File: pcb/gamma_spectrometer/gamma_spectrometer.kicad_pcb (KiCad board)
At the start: 4 copper layers, 45 x 45 mm, 186 parts, among them J101 DX07S024WJ3R400, Q201 IRLML0040, Q401 MMBTA42, Q402 MMBTA42, Q403 MMBTA42, T201 ATB322524-0110-T000, U101 LP5907MFX-3.3, U102 AMS1117-3.3, U103 FT231XQ, U104 TPS60400DBV, U201 max1847eee+, U202 TL431, U301 TL431, U302 STM32G474MET6, U303 W25Q64JVSSIQ, U401 AD8000YRDZ-REEL, Y301 ABM8G-16.000MHZ-4Y-T3

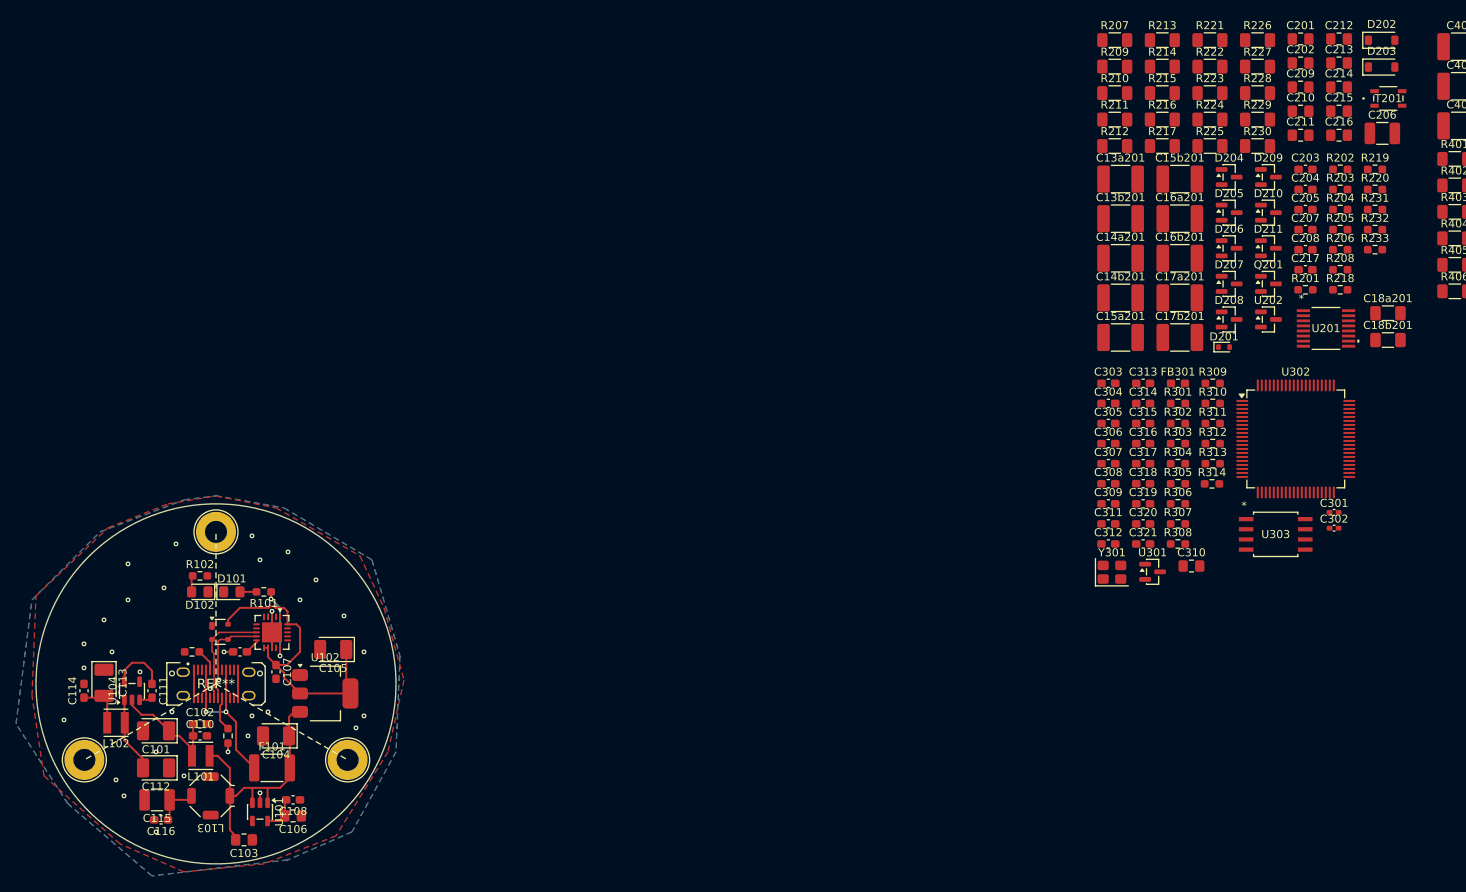
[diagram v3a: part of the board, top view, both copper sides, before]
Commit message: pcb: разводка HV + GND-полигоны + межплатная шина (HV/USB)
- HV-плата разведена (накопит. конденсаторы и монитор-делитель вынесены вниз),
  GND залит полигонами, паритет со схемой 0.
- USB: добавлен GND-план на In2.Cu (второй внутренний слой), сшивка.
- Межплатная шина цанг-пинов: по 13 пинов на HV и USB, выровнены на R20
  равным шагом 13° с разрывами под стойки (120°/240°); углы идентичны на
  обеих платах -> соосность через стек.
- DRC (headless, с заливкой зон): паритет со схемой 0 на обеих платах;
  остатки минорные (1-2 GND-хвоста, courtyard-грейзы пин/стойка, silk, REF**).

Co-Authored-By: Claude Opus 4.8 <noreply@anthropic.com>
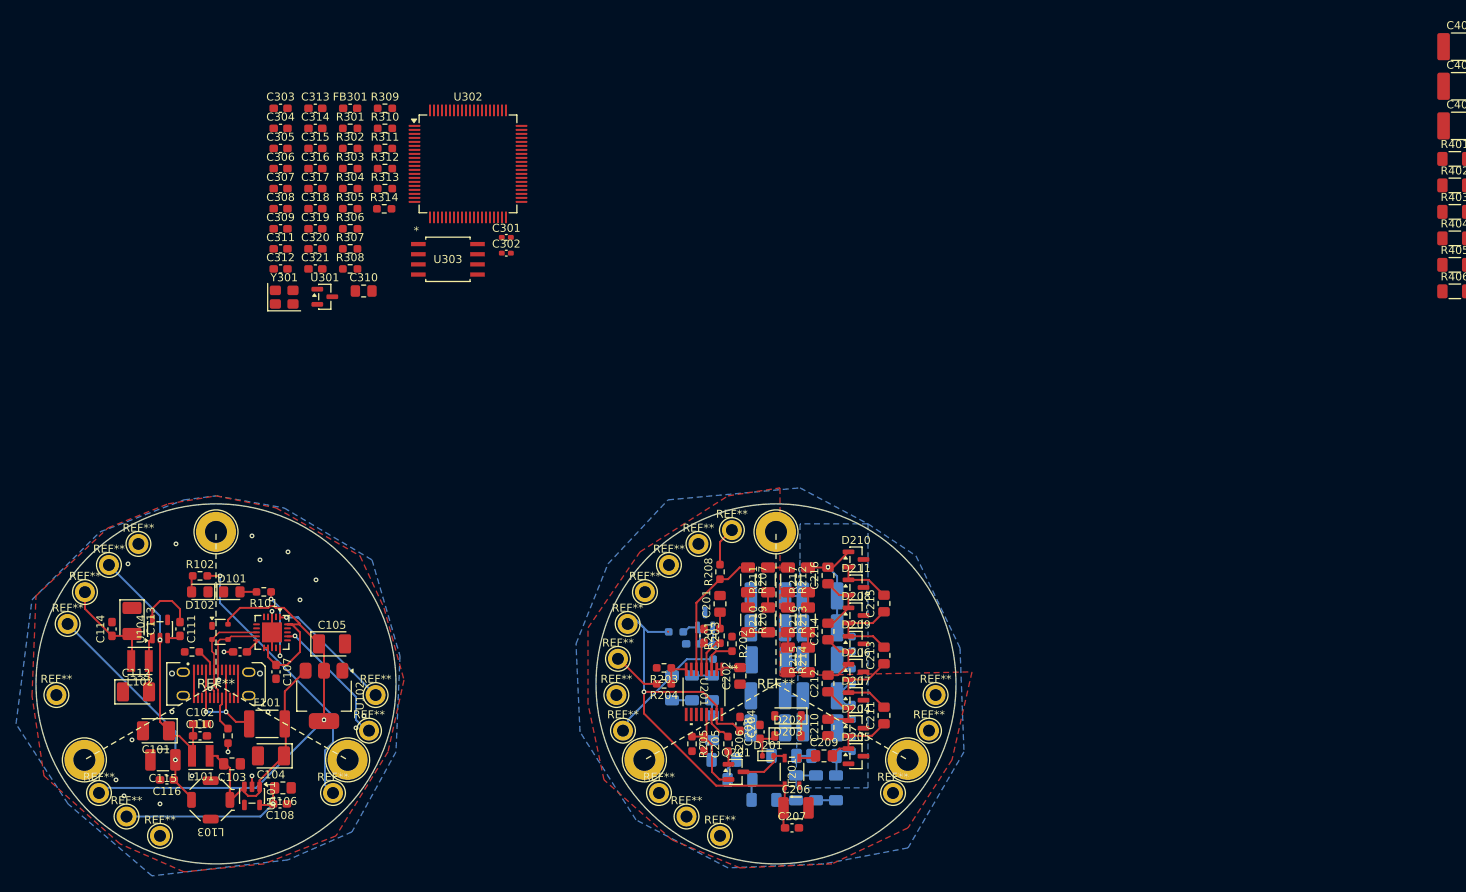
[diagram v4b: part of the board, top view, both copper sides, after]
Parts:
- added REF**: INTERCONNECT_PIN_D1.5, посадочные места:INTERCONNECT_PIN_D1.5, F.Cu at (156.6, 85.1)
- added REF**: INTERCONNECT_PIN_D1.5, посадочные места:INTERCONNECT_PIN_D1.5, F.Cu at (80.0, 101.4)
- added REF**: INTERCONNECT_PIN_D1.5, посадочные места:INTERCONNECT_PIN_D1.5, F.Cu at (114.6, 113.6)
- added REF**: INTERCONNECT_PIN_D1.5, посадочные места:INTERCONNECT_PIN_D1.5, F.Cu at (86.6, 85.1)
- added REF**: INTERCONNECT_PIN_D1.5, посадочные места:INTERCONNECT_PIN_D1.5, F.Cu at (150.9, 105.8)
- added REF**: INTERCONNECT_PIN_D1.5, посадочные места:INTERCONNECT_PIN_D1.5, F.Cu at (150.0, 101.4)
- added REF**: STANDOFF_M2.5_GND_x3_TRIANGLE, посадочные места:STANDOFF_M2.5_GND_x3_TRIANGLE, F.Cu at (170.0, 100.0)
- added REF**: INTERCONNECT_PIN_D1.5, посадочные места:INTERCONNECT_PIN_D1.5, F.Cu at (160.3, 82.5)
- added REF**: INTERCONNECT_PIN_D1.5, посадочные места:INTERCONNECT_PIN_D1.5, F.Cu at (190.0, 101.4)
- added REF**: INTERCONNECT_PIN_D1.5, посадочные места:INTERCONNECT_PIN_D1.5, F.Cu at (184.6, 113.6)
- added REF**: INTERCONNECT_PIN_D1.5, посадочные места:INTERCONNECT_PIN_D1.5, F.Cu at (120.0, 101.4)
- added REF**: INTERCONNECT_PIN_D1.5, посадочные места:INTERCONNECT_PIN_D1.5, F.Cu at (164.5, 80.8)
- added REF**: INTERCONNECT_PIN_D1.5, посадочные места:INTERCONNECT_PIN_D1.5, F.Cu at (88.8, 116.6)
- added REF**: INTERCONNECT_PIN_D1.5, посадочные места:INTERCONNECT_PIN_D1.5, F.Cu at (153.6, 88.5)
- added REF**: INTERCONNECT_PIN_D1.5, посадочные места:INTERCONNECT_PIN_D1.5, F.Cu at (81.5, 92.5)
- added REF**: INTERCONNECT_PIN_D1.5, посадочные места:INTERCONNECT_PIN_D1.5, F.Cu at (90.3, 82.5)
- added REF**: INTERCONNECT_PIN_D1.5, посадочные места:INTERCONNECT_PIN_D1.5, F.Cu at (189.1, 105.8)
- added REF**: INTERCONNECT_PIN_D1.5, посадочные места:INTERCONNECT_PIN_D1.5, F.Cu at (163.0, 119.0)
- added REF**: INTERCONNECT_PIN_D1.5, посадочные места:INTERCONNECT_PIN_D1.5, F.Cu at (150.2, 96.9)
- added REF**: INTERCONNECT_PIN_D1.5, посадочные места:INTERCONNECT_PIN_D1.5, F.Cu at (83.6, 88.5)
- added REF**: INTERCONNECT_PIN_D1.5, посадочные места:INTERCONNECT_PIN_D1.5, F.Cu at (158.8, 116.6)
- added REF**: INTERCONNECT_PIN_D1.5, посадочные места:INTERCONNECT_PIN_D1.5, F.Cu at (155.4, 113.6)
- added REF**: INTERCONNECT_PIN_D1.5, посадочные места:INTERCONNECT_PIN_D1.5, F.Cu at (85.4, 113.6)
- added REF**: INTERCONNECT_PIN_D1.5, посадочные места:INTERCONNECT_PIN_D1.5, F.Cu at (119.1, 105.8)
- added REF**: INTERCONNECT_PIN_D1.5, посадочные места:INTERCONNECT_PIN_D1.5, F.Cu at (93.0, 119.0)
- added REF**: INTERCONNECT_PIN_D1.5, посадочные места:INTERCONNECT_PIN_D1.5, F.Cu at (151.5, 92.5)
- C13a201, C13b201, C14a201, C14b201, C15a201, C15b201, C16a201, C16b201, C17a201, C17b201, C18a201, C18b201, C217, R218, R219, R220, R221, R222, R223, R224, R225, R226, R227, R228, R229, R230, R231, R232, R233, U202: moved to B.Cu
- moved D202 114.3 mm to (171.5, 106.5)
- moved T201 112.4 mm to (172.0, 111.0), turned to 90 degrees
- moved R226 112.0 mm to (163.5, 109.5), turned to 180 degrees
- moved C206 111.7 mm to (172.5, 115.5)
- moved D203 109.9 mm to (171.5, 104.0), turned to 180 degrees
- moved U303 109.0 mm to (129.0, 46.9)
- moved C310 109.0 mm to (118.5, 50.9)
- moved C313 109.0 mm to (112.4, 28.1)
- moved C314 109.0 mm to (112.4, 30.6)
- moved C315 109.0 mm to (112.4, 33.1)
- moved C316 109.0 mm to (112.4, 35.6)
- moved C317 109.0 mm to (112.4, 38.1)
- moved C318 109.0 mm to (112.4, 40.6)
- moved C319 109.0 mm to (112.4, 43.1)
- moved C320 109.0 mm to (112.4, 45.6)
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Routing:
- net +5V_HV: track 5.53 -> 88.5 mm, vias 0 -> 2
- net LED: track 0.00 -> 35.4 mm, vias 0 -> 1
- net +3.3V_D: track 38.9 -> 69.1 mm, vias 0 -> 1
- net +3.3V_A: track 4.49 -> 22.8 mm, vias 0 -> 1
- net +5V_A: track 16.1 -> 33.5 mm, vias 0 -> 1
- net UART_TX: track 0.00 -> 16.8 mm, vias 0 -> 1
- net Net-(U201-FB): track 0.00 -> 16.6 mm
- net Net-(C13a201-Pad1): track 0.00 -> 16.2 mm, vias 0 -> 1
- net UART_RX: track 0.00 -> 16.1 mm, vias 0 -> 1
- net HV_MONITOR: track 0.00 -> 15.5 mm
- net Net-(C211-Pad2): track 0.00 -> 12.1 mm
- net Net-(Q201-S): track 0.00 -> 11.7 mm
- net Net-(C213-Pad2): track 0.00 -> 11.7 mm
- net Net-(C209-Pad2): track 0.00 -> 9.08 mm
- net Net-(C214-Pad2): track 0.00 -> 8.10 mm
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- added copper zone on In2.Cu, net GND
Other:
- board size 45 x 45 mm -> 115 x 45 mm

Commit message: pcb: ВВ-зазоры 3 мм/кВ правилами DRC + 2 слоя + разводка делителя
Плата переведена 4 -> 2 слоя (ЛУТ-прототипы): на In1/In2 разводки не было,
удалены только зоны, связность не изменилась (178 несоединённых до и после).
Стек F.Cu / core FR4 1.51 / B.Cu = 1.60 мм. Побочно снят риск: под -1500 В
лежала сплошная земля через препрег 0.1 мм (15 кВ/мм), стало 0.99 кВ/мм.

Нормы ВВ-зазоров заданы правилами DRC (gamma_spectrometer.kicad_dru):
49 правил "ВВ-цепь <-> GND" по 3 мм на 1 кВ + 12 исключений. Потенциалы
посчитаны из топологии: рабочая точка делителя, порядок лестницы CW по
диодам (8 ступеней по 189 В), падения на выходном RC, цепочки ОС и монитора.
Зазоры 4.54 мм (CW_out, 1514 В) ... 0.43 мм. Ограничивают только пару с GND —
между соседними ступенями ВВ разность 150-190 В (принцип градиента).

Исключения: 12 компонентов по схеме соединяют ВВ-узел с землёй (T201, C210,
D205, C410, R412, C13b-C18b201, Q403). У них зазор задан корпусом детали и
перемещением не лечится; прочность держит рабочее напряжение компонента.
R412 при этом на 98% от рейтинга (196 В при 200 В) — кандидат на деление
на два по 1 МОм.

Итог: ВВ-нарушений 357 -> 0, всего 774 -> 416, категория clearance пуста.

Расстановка:
- контуры МК (240,100) и делителя (310,100), стойки GND на всех 4 платах
- J_PMT401 на делителе, поворот -69° подобран перебором по ВВ-зазорам
  (узкое место Dy7: 1.74 мм при требуемых 0.79, минимальный запас +0.95)
- межплатные посадки выровнены на дугу R=20 и соосны: -HV_out 72°, AMP_OUT 325°
- на МК цанга -HV_out заменена сквозным отверстием Ø5 NPTH (H_HV301):
  провод -ВВ идёт мимо платы МК, как и задумано в доках
- шина скопирована с USB на делитель; board_only всем 43 механическим футпринтам
- удалено 13 футпринтов старого делителя (вкл. дубль R408) и 10 GND-виа
- проектная копия футпринта USB-C с падами экрана 25-28 вместо S1
  (экран разъёма висел без цепи)

Симуляции:
- найдена недостоверная метрика пиковости в sim_tia_stab.cir (делила дБ на дБ):
  рапортовала -49.7 дБ там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
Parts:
- removed C401, C402, C403, C404, C405, C406, C407: 0.1uF, Capacitor_SMD:C_1812_4532Metric_Pad1.57x3.40mm_HandSolder
- removed R411, R413: 10k, Resistor_SMD:R_0603_1608Metric_Pad0.98x0.95mm_HandSolder
- removed R414: 499k, Resistor_SMD:R_1206_3216Metric_Pad1.30x1.75mm_HandSolder
- removed R415: 49.9, Resistor_SMD:R_0603_1608Metric_Pad0.98x0.95mm_HandSolder
- removed R416: 100, Resistor_SMD:R_0603_1608Metric_Pad0.98x0.95mm_HandSolder
- removed U401: AD8000YRDZ-REEL, посадочные места:RD_8_1_ADI-M
- added D401: 1N4148W, Diode_SMD:D_SOD-123, B.Cu at (305.5, 94.0)
- added D402: 1N4148W, Diode_SMD:D_SOD-123, B.Cu at (309.0, 90.5)
- added D403: 1N4148W, Diode_SMD:D_SOD-123, B.Cu at (313.0, 94.0)
- added H_HV301: HOLE_HV_WIRE_D5.0, HOLE_HV_WIRE_D5.0, F.Cu at (245.6, 117.1)
- added J_PMT401: PMT, посадочные места:J_PMT401_R1307-01, F.Cu at (310.0, 100.0)
- added REF**: INTERCONNECT_PIN_D1.5, посадочные места:INTERCONNECT_PIN_D1.5, F.Cu at (220.0, 101.4)
- added REF**: INTERCONNECT_PIN_D1.5, INTERCONNECT_PIN_D1.5, F.Cu at (300.3, 82.5)
- added REF**: INTERCONNECT_PIN_D1.5, посадочные места:INTERCONNECT_PIN_D1.5, F.Cu at (176.2, 119.0)
- added REF**: INTERCONNECT_PIN_D1.5, посадочные места:INTERCONNECT_PIN_D1.5, F.Cu at (220.2, 96.9)
- added REF**: STANDOFF_M2.5_GND_x3_TRIANGLE, посадочные места:STANDOFF_M2.5_GND_x3_TRIANGLE, F.Cu at (240.0, 100.0)
- added REF**: INTERCONNECT_PIN_D1.5, посадочные места:INTERCONNECT_PIN_D1.5, F.Cu at (234.5, 80.8)
- added REF**: INTERCONNECT_PIN_D1.5, посадочные места:INTERCONNECT_PIN_D1.5, F.Cu at (316.2, 119.0)
- added REF**: INTERCONNECT_PIN_D1.5, посадочные места:INTERCONNECT_PIN_D1.5, F.Cu at (233.2, 118.8)
- added REF**: INTERCONNECT_PIN_D1.5, INTERCONNECT_PIN_D1.5, F.Cu at (296.6, 85.1)
- added REF**: INTERCONNECT_PIN_D1.5, посадочные места:INTERCONNECT_PIN_D1.5, F.Cu at (228.8, 116.6)
- added REF**: INTERCONNECT_PIN_D1.5, посадочные места:INTERCONNECT_PIN_D1.5, F.Cu at (309.0, 99.5)
- added REF**: INTERCONNECT_PIN_D1.5, INTERCONNECT_PIN_D1.5, F.Cu at (303.2, 118.8)
- added REF**: INTERCONNECT_PIN_D1.5, посадочные места:INTERCONNECT_PIN_D1.5, F.Cu at (226.6, 85.1)
- added REF**: INTERCONNECT_PIN_D1.5, INTERCONNECT_PIN_D1.5, F.Cu at (293.6, 88.5)
- added REF**: INTERCONNECT_PIN_D1.5, посадочные места:INTERCONNECT_PIN_D1.5, F.Cu at (220.9, 105.8)
- added REF**: INTERCONNECT_PIN_D1.5, посадочные места:INTERCONNECT_PIN_D1.5, F.Cu at (225.4, 113.6)
- added REF**: INTERCONNECT_PIN_D1.5, посадочные места:INTERCONNECT_PIN_D1.5, F.Cu at (230.3, 82.5)
- added REF**: STANDOFF_M2.5_GND_x3_TRIANGLE, посадочные места:STANDOFF_M2.5_GND_x3_TRIANGLE, F.Cu at (310.0, 100.0)
- added REF**: INTERCONNECT_PIN_D1.5, посадочные места:INTERCONNECT_PIN_D1.5, F.Cu at (259.1, 105.8)
- added REF**: INTERCONNECT_PIN_D1.5, посадочные места:INTERCONNECT_PIN_D1.5, F.Cu at (260.0, 101.4)
- added REF**: INTERCONNECT_PIN_D1.5, посадочные места:INTERCONNECT_PIN_D1.5, F.Cu at (243.5, 84.5)
- added REF**: INTERCONNECT_PIN_D1.5, посадочные места:INTERCONNECT_PIN_D1.5, F.Cu at (223.6, 88.5)
- added REF**: INTERCONNECT_PIN_D1.5, посадочные места:INTERCONNECT_PIN_D1.5, F.Cu at (254.6, 113.6)
- added U402: ADA4817-1ARDZ, посадочные места:RD_8_1_ADI-M, F.Cu at (317.0, 102.0)
- C304, Q401, Q402, Q403: moved to B.Cu
- C415: value 1pF -> 4.7pF
- R407: value 680k -> 1.3M
- R408: value 10k -> 1.3M; footprint Resistor_SMD:R_0603_1608Metric_Pad0.98x0.95mm_HandSolder -> Resistor_SMD:R_1206_3216Metric_Pad1.30x1.75mm_HandSolder
- R409: value 820k -> 1.6M
- R410, R412: value 1M -> 2M
- R417: value 1.5k -> 499
- moved C307 156.0 mm to (249.0, 105.0), turned to -90 degrees
- moved C319 155.2 mm to (254.5, 105.5), turned to 180 degrees
- moved C306 151.2 mm to (240.0, 109.5), turned to -90 degrees
- moved C308 151.0 mm to (248.5, 96.0), turned to -90 degrees
- moved C312 149.5 mm to (244.0, 110.4), turned to 90 degrees
- moved C305 148.2 mm to (235.0, 109.5), turned to -90 degrees
- moved C309 147.6 mm to (247.0, 93.0)
- moved R302 147.6 mm to (242.5, 110.4), turned to -90 degrees
- moved Y301 142.8 mm to (246.2, 89.6), turned to 90 degrees
- moved C304 141.3 mm to (236.0, 90.5), turned to 180 degrees
- moved C317 139.4 mm to (241.4, 91.0)
- moved C303 137.8 mm to (226.4, 98.6)
- moved C315 136.8 mm to (237.0, 89.6), turned to -90 degrees
- moved FB301 136.2 mm to (229.5, 104.5), turned to 90 degrees
- moved C314 136.2 mm to (234.0, 91.9), turned to 90 degrees
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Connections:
- C408 pad 1: /Divider_Board/DY5 -> /Divider_Board/DY6
- C408 pad 2: /Divider_Board/DY6 -> /Divider_Board/DY7
- C409 pad 1: /Divider_Board/DY6 -> /Divider_Board/DY7
- C409 pad 2: /Divider_Board/DY7 -> /Divider_Board/DY8
- C410 pad 1: /Divider_Board/DY7 -> /Divider_Board/DY8
- C410 pad 2: /Divider_Board/DY8 -> GND
- C415 pad 1: AMP_OUT -> /Divider_Board/P
- C415 pad 2: Net-(U401-FEEDBACK) -> FeedBack
- Q401 pad 1: Net-(Q401-B) -> Net-(D401-K)
- Q402 pad 1: Net-(Q402-B) -> Net-(D402-K)
- Q403 pad 1: Net-(Q403-B) -> Net-(D403-K)
- R407 pad 2: Net-(C407-Pad2) -> Net-(D401-K)
- R408 pad 1: Net-(Q401-B) -> /Divider_Board/DY5
- R408 pad 2: Net-(C407-Pad2) -> /Divider_Board/DY6
- R409 pad 1: Net-(C407-Pad2) -> Net-(D401-K)
- R409 pad 2: Net-(R409-Pad2) -> Net-(D402-K)
- R410 pad 1: Net-(R409-Pad2) -> Net-(D402-K)
- R410 pad 2: Net-(R410-Pad2) -> Net-(D403-K)
- R412 pad 1: Net-(R410-Pad2) -> Net-(D403-K)
- R417 pad 1: AMP_OUT -> FeedBack
- R417 pad 2: Net-(U401-FEEDBACK) -> /Divider_Board/P
- REF** pad 1: (no net) -> GND
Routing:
- net +3.3V_D: track 69.1 -> 161.7 mm, vias 1 -> 7
- net −5V_A: track 13.5 -> 63.7 mm, vias 0 -> 1
- net +5V_A: track 33.5 -> 68.5 mm, vias 1 -> 2
- net Net-(C312-Pad1): track 0.00 -> 32.5 mm, vias 0 -> 2
- net HV_MONITOR: track 15.5 -> 46.0 mm
- net +3.3V_A: track 22.8 -> 47.0 mm, vias 1 -> 3
- net LED: track 35.4 -> 56.1 mm, vias 1 -> 3
- net Net-(U302-PA5): track 0.00 -> 20.1 mm, vias 0 -> 6
- net UART_RX: track 16.1 -> 36.2 mm, vias 1 -> 2
- net UART_TX: track 16.8 -> 34.2 mm, vias 1 -> 2
- net /Divider_Board/DY8: track 0.00 -> 16.3 mm, vias 0 -> 1
- net HV_ENABLE: track 6.83 -> 23.0 mm, vias 0 -> 2
- net −HV_out: track 4.66 -> 20.1 mm
- net /Divider_Board/DY7: track 0.00 -> 14.4 mm, vias 0 -> 1
- net SPI_CS: track 0.00 -> 14.3 mm, vias 0 -> 2
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- removed copper zone on In1.Cu, net GND
- removed copper zone on In2.Cu, net GND
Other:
- board size 115 x 45 mm -> 255 x 45 mm
- copper layers 4 -> 2
